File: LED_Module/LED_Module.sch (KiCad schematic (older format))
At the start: 12 parts, among them P1 CONN_01X03, P2 CONN_01X01, P3 CONN_01X01, U1 AL8805WS

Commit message: PCB square shape
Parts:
- removed D2: LED, KiCad_Footprint:Power_LED, symbol LED
- removed P1: CONN_01X03, Connectors_JST:JST_XH_B03B-XH-A_03x2.50mm_Straight, symbol CONN_01X03
- added P1, P4, P5: CONN_01X01, Socket_Strips:Socket_Strip_Straight_1x01, symbol CONN_01X01
- P2, P3: footprint Wire_Pads:SolderWirePad_single_1-2mmDrill -> Socket_Strips:Socket_Strip_Straight_1x01
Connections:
- wire segments 24 -> 19
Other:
- moved on the sheet: C2, C3, D1
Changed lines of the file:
@@
 L ZENER D1
 U 1 1 580A76F9
-P 6850 2850
-F 0 "D1" H 6850 2950 50  0000 C CNN
-F 1 "BAT20JFILM" H 6850 2750 50  0000 C CNN
-F 2 "w_smd_diode:sod323" H 6850 2850 50  0001 C CNN
-F 3 "" H 6850 2850 50  0000 C CNN
-	1    6850 2850
+P 6850 3100
+F 0 "D1" H 6850 3200 50  0000 C CNN
+F 1 "BAT20JFILM" H 6850 3000 50  0000 C CNN
+F 2 "w_smd_diode:sod323" H 6850 3100 50  0001 C CNN
+F 3 "" H 6850 3100 50  0000 C CNN
+	1    6850 3100
 	0    1    1    0
 $EndComp
@@
 $EndComp
 $Comp
-L C C3
-U 1 1 580A8826
-P 7150 2350
-F 0 "C3" H 7175 2450 50  0000 L CNN
-F 1 "2.2uF" H 7175 2250 50  0000 L CNN
-F 2 "Capacitors_SMD:C_0805_HandSoldering" H 7188 2200 50  0001 C CNN
-F 3 "" H 7150 2350 50  0000 C CNN
-	1    7150 2350
-	0    1    1    0
-$EndComp
-$Comp
 L GND #PWR02
 U 1 1 580A8863
-P 7400 2350
-F 0 "#PWR02" H 7400 2100 50  0001 C CNN
-F 1 "GND" H 7400 2200 50  0000 C CNN
-F 2 "" H 7400 2350 50  0000 C CNN
-F 3 "" H 7400 2350 50  0000 C CNN
-	1    7400 2350
+P 7375 2550
+F 0 "#PWR02" H 7375 2300 50  0001 C CNN
+F 1 "GND" H 7375 2400 50  0000 C CNN
+F 2 "" H 7375 2550 50  0000 C CNN
+F 3 "" H 7375 2550 50  0000 C CNN
+	1    7375 2550
 	1    0    0    -1
 $EndComp
 Text Label 3850 2550 0    60   ~ 0
 CTRL_PWM
-Text Label 5000 2150 0    60   ~ 0
+Text Label 4825 2150 0    60   ~ 0
 V_BAT
 $Comp
@@
 Connection ~ 6050 3150
 Wire Wire Line
-	6850 3050 6850 3675
-Wire Wire Line
-	5900 2550 5900 2350
-Wire Wire Line
-	5900 2350 7000 2350
-Wire Wire Line
-	6850 2350 6850 2650
-Connection ~ 5900 2550
-Connection ~ 6850 2350
-Wire Wire Line
-	7400 2350 7300 2350
+	7250 2550 7375 2550
 Wire Wire Line
 	5500 2150 5500 2550
 Wire Wire Line
-	5000 2150 5500 2150
+	4825 2150 5500 2150
 Connection ~ 5500 2550
 Wire Wire Line
@@
 	5350 2850 6625 2850
 Wire Wire Line
-	5350 2550 6000 2550
+	5350 2550 6950 2550
 Wire Wire Line
 	5400 3450 5400 3675
@@
 	5400 3675 6850 3675
 Connection ~ 5400 3450
-$Comp
-L CONN_01X03 P1
-U 1 1 58228E03
-P 4925 4675
-F 0 "P1" H 4925 4875 50  0000 C CNN
-F 1 "CONN_01X03" V 5025 4675 50  0000 C CNN
-F 2 "Connectors_JST:JST_XH_B03B-XH-A_03x2.50mm_Straight" H 4925 4675 50  0001 C CNN
-F 3 "" H 4925 4675 50  0000 C CNN
-	1    4925 4675
-	1    0    0    -1
-$EndComp
-Text Label 4050 4675 0    60   ~ 0
+Text Label 3975 4750 0    60   ~ 0
 V_BAT
 $Comp
 L GND #PWR05
 U 1 1 58229257
-P 4050 4575
-F 0 "#PWR05" H 4050 4325 50  0001 C CNN
-F 1 "GND" H 4050 4425 50  0000 C CNN
-F 2 "" H 4050 4575 50  0000 C CNN
-F 3 "" H 4050 4575 50  0000 C CNN
-	1    4050 4575
-	0    1    1    0
-$EndComp
-Wire Wire Line
-	4050 4675 4725 4675
-Text Label 4050 4775 0    60   ~ 0
+P 3975 4200
+F 0 "#PWR05" H 3975 3950 50  0001 C CNN
+F 1 "GND" H 3975 4050 50  0000 C CNN
+F 2 "" H 3975 4200 50  0000 C CNN
+F 3 "" H 3975 4200 50  0000 C CNN
+	1    3975 4200
+	0    1    1    0
+$EndComp
+Wire Wire Line
+	3975 4750 4650 4750
+Text Label 3975 4475 0    60   ~ 0
 CTRL_PWM
 Wire Wire Line
-	4725 4775 4050 4775
-Wire Wire Line
-	4725 4575 4050 4575
-$Comp
-L LED D2
-U 1 1 582297B2
-P 6350 4625
-F 0 "D2" H 6350 4725 50  0000 C CNN
-F 1 "LED" H 6350 4525 50  0000 C CNN
-F 2 "KiCad_Footprint:Power_LED" H 6350 4800 50  0001 C CNN
-F 3 "" H 6350 4625 50  0000 C CNN
-	1    6350 4625
-	-1   0    0    1
-$EndComp
-Wire Wire Line
-	6150 4625 5600 4625
-Wire Wire Line
-	6550 4625 7150 4625
-Text Label 5900 4625 2    60   ~ 0
-LED1-
-Text Label 7150 4625 2    60   ~ 0
-LED1+
+	4650 4475 3975 4475
+Wire Wire Line
+	4650 4200 3975 4200
 $Comp
 L C C2
 U 1 1 5822AADF
-P 4625 5025
-F 0 "C2" H 4650 5125 50  0000 L CNN
-F 1 "C" H 4650 4925 50  0000 L CNN
-F 2 "Capacitors_SMD:c_elec_5x4.5" H 4663 4875 50  0001 C CNN
-F 3 "" H 4625 5025 50  0000 C CNN
-	1    4625 5025
+P 4550 4900
+F 0 "C2" H 4575 5000 50  0000 L CNN
+F 1 "C" H 4575 4800 50  0000 L CNN
+F 2 "Capacitors_SMD:c_elec_5x4.5" H 4588 4750 50  0001 C CNN
+F 3 "" H 4550 4900 50  0000 C CNN
+	1    4550 4900
 	1    0    0    -1
 $EndComp
@@
 L GND #PWR06
 U 1 1 5822AB43
-P 4625 5175
-F 0 "#PWR06" H 4625 4925 50  0001 C CNN
-F 1 "GND" H 4625 5025 50  0000 C CNN
-F 2 "" H 4625 5175 50  0000 C CNN
-F 3 "" H 4625 5175 50  0000 C CNN
-	1    4625 5175
-	1    0    0    -1
-$EndComp
-Wire Wire Line
-	4625 4675 4625 4875
-Connection ~ 4625 4675
+P 4550 5050
+F 0 "#PWR06" H 4550 4800 50  0001 C CNN
+F 1 "GND" H 4550 4900 50  0000 C CNN
+F 2 "" H 4550 5050 50  0000 C CNN
+F 3 "" H 4550 5050 50  0000 C CNN
+	1    4550 5050
+	1    0    0    -1
+$EndComp
+Connection ~ 4550 4750
+$Comp
+L CONN_01X01 P1
+U 1 1 58242D49
+P 4850 4200
+F 0 "P1" H 4850 4300 50  0000 C CNN
+F 1 "CONN_01X01" H 5275 4200 50  0000 C CNN
+F 2 "Socket_Strips:Socket_Strip_Straight_1x01" H 4850 4200 50  0001 C CNN
+F 3 "" H 4850 4200 50  0000 C CNN
+	1    4850 4200
+	1    0    0    -1
+$EndComp
 $Comp
 L CONN_01X01 P2
-U 1 1 5822A57E
-P 5975 5175
-F 0 "P2" H 5975 5275 50  0000 C CNN
-F 1 "CONN_01X01" V 6075 5175 50  0000 C CNN
-F 2 "Wire_Pads:SolderWirePad_single_1-2mmDrill" H 5975 5175 50  0001 C CNN
-F 3 "" H 5975 5175 50  0000 C CNN
-	1    5975 5175
+U 1 1 58242E95
+P 4850 4750
+F 0 "P2" H 4850 4850 50  0000 C CNN
+F 1 "CONN_01X01" H 5275 4750 50  0000 C CNN
+F 2 "Socket_Strips:Socket_Strip_Straight_1x01" H 4850 4750 50  0001 C CNN
+F 3 "" H 4850 4750 50  0000 C CNN
+	1    4850 4750
 	1    0    0    -1
 $EndComp
 $Comp
 L CONN_01X01 P3
-U 1 1 5822A779
-P 7000 5150
-F 0 "P3" H 7000 5250 50  0000 C CNN
-F 1 "CONN_01X01" V 7100 5150 50  0000 C CNN
-F 2 "Wire_Pads:SolderWirePad_single_1-2mmDrill" H 7000 5150 50  0001 C CNN
-F 3 "" H 7000 5150 50  0000 C CNN
-	1    7000 5150
-	1    0    0    -1
-$EndComp
-Text Label 5650 5175 2    60   ~ 0
+U 1 1 58242EC7
+P 4850 4475
+F 0 "P3" H 4850 4575 50  0000 C CNN
+F 1 "CONN_01X01" H 5275 4475 50  0000 C CNN
+F 2 "Socket_Strips:Socket_Strip_Straight_1x01" H 4850 4475 50  0001 C CNN
+F 3 "" H 4850 4475 50  0000 C CNN
+	1    4850 4475
+	1    0    0    -1
+$EndComp
+$Comp
+L CONN_01X01 P4
+U 1 1 58243C3A
+P 6725 4200
+F 0 "P4" H 6725 4300 50  0000 C CNN
+F 1 "CONN_01X01" H 7075 4200 50  0000 C CNN
+F 2 "Socket_Strips:Socket_Strip_Straight_1x01" H 6725 4200 50  0001 C CNN
+F 3 "" H 6725 4200 50  0000 C CNN
+	1    6725 4200
+	1    0    0    -1
+$EndComp
+$Comp
+L CONN_01X01 P5
+U 1 1 58243CBE
+P 6725 4475
+F 0 "P5" H 6725 4575 50  0000 C CNN
+F 1 "CONN_01X01" H 7075 4475 50  0000 C CNN
+F 2 "Socket_Strips:Socket_Strip_Straight_1x01" H 6725 4475 50  0001 C CNN
+F 3 "" H 6725 4475 50  0000 C CNN
+	1    6725 4475
+	1    0    0    -1
+$EndComp
+Wire Wire Line
+	6525 4200 5850 4200
+Wire Wire Line
+	6525 4475 5850 4475
+Text Label 6150 4200 2    60   ~ 0
 LED1+
-Text Label 6600 5150 2    60   ~ 0
+Text Label 6150 4475 2    60   ~ 0
 LED1-
-Wire Wire Line
-	5775 5175 5350 5175
-Wire Wire Line
-	6800 5150 6325 5150
+$Comp
+L C C3
+U 1 1 580A8826
+P 7100 2550
+F 0 "C3" H 7125 2650 50  0000 L CNN
+F 1 "2.2uF" H 7125 2450 50  0000 L CNN
+F 2 "Capacitors_SMD:C_0805_HandSoldering" H 7138 2400 50  0001 C CNN
+F 3 "" H 7100 2550 50  0000 C CNN
+	1    7100 2550
+	0    1    1    0
+$EndComp
+Connection ~ 6000 2550
+Wire Wire Line
+	6850 3675 6850 3300
+Wire Wire Line
+	6850 2900 6850 2550
+Connection ~ 6850 2550
 $EndSCHEMATC

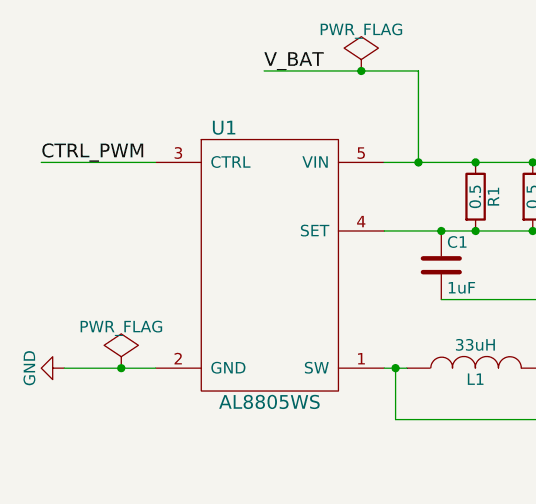
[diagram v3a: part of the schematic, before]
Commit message: LED Module PWM pull down
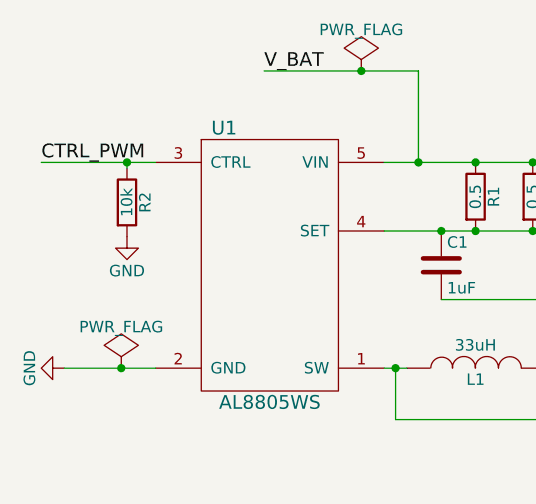
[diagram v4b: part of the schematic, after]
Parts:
- added R2: 10k, Resistors_SMD:R_0805_HandSoldering, symbol R
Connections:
- wire segments 19 -> 20
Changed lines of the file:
@@
 	6850 2900 6850 2550
 Connection ~ 6850 2550
+$Comp
+L R R2
+U 1 1 58281BBD
+P 4225 2725
+F 0 "R2" V 4305 2725 50  0000 C CNN
+F 1 "10k" V 4225 2725 50  0000 C CNN
+F 2 "Resistors_SMD:R_0805_HandSoldering" V 4155 2725 50  0001 C CNN
+F 3 "" H 4225 2725 50  0000 C CNN
+	1    4225 2725
+	1    0    0    -1
+$EndComp
+Wire Wire Line
+	4225 2550 4225 2575
+Connection ~ 4225 2550
+$Comp
+L GND #PWR07
+U 1 1 58281D10
+P 4225 2875
+F 0 "#PWR07" H 4225 2625 50  0001 C CNN
+F 1 "GND" H 4225 2725 50  0000 C CNN
+F 2 "" H 4225 2875 50  0000 C CNN
+F 3 "" H 4225 2875 50  0000 C CNN
+	1    4225 2875
+	1    0    0    -1
+$EndComp
 $EndSCHEMATC
